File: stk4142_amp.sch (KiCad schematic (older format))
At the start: 6 parts

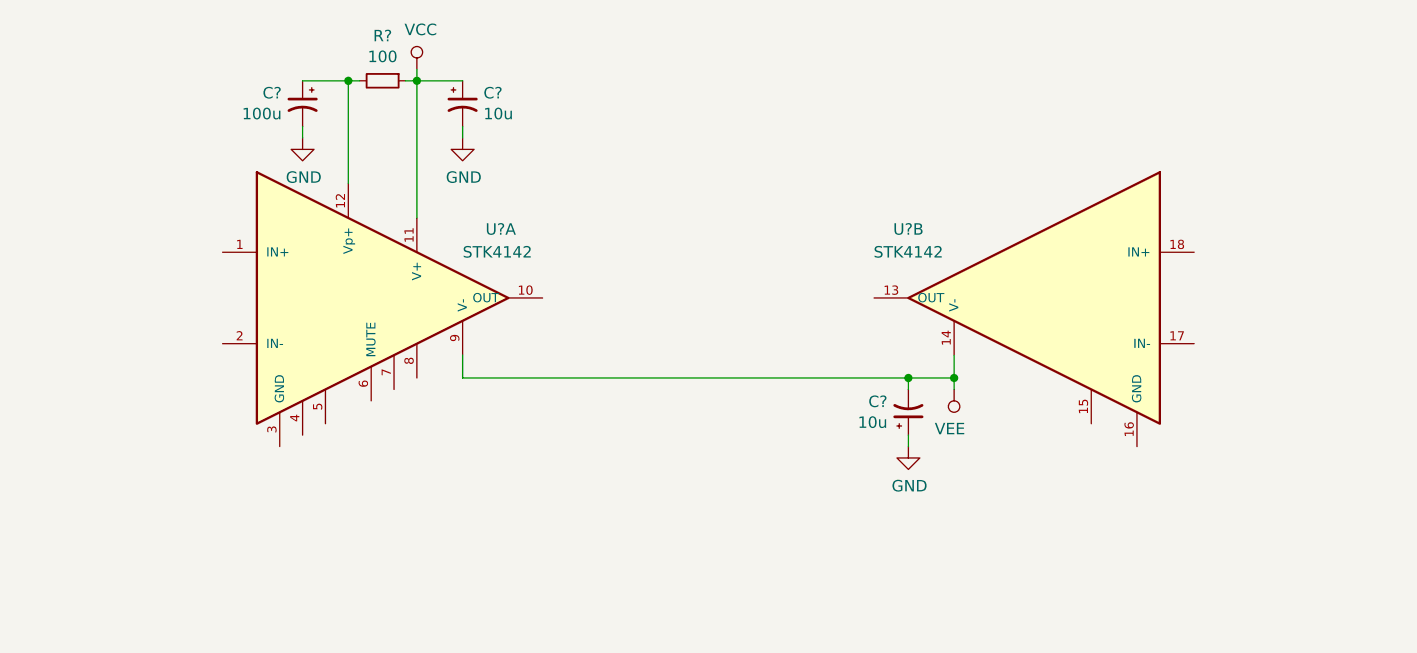
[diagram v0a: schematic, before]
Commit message: main elements of power stage
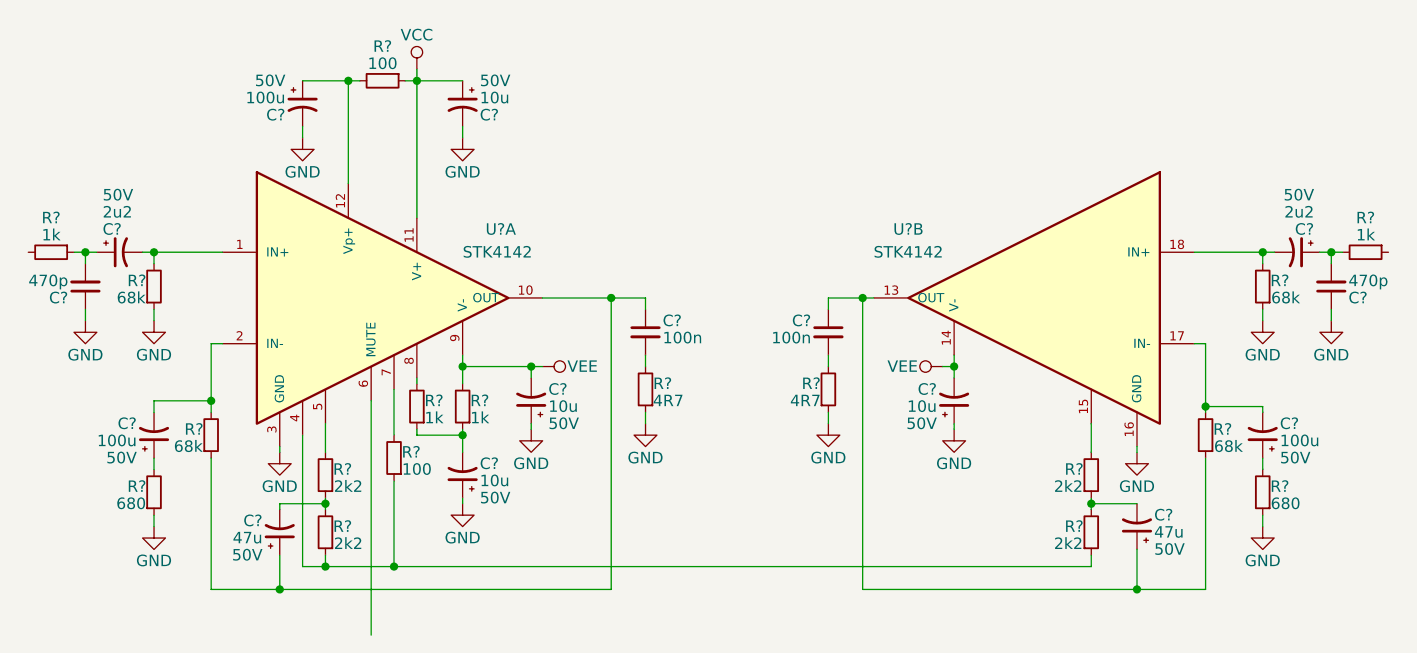
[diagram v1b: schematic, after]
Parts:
- removed C?: 100u, symbol CP1_Small
- removed C? (x2): 10u, symbol CP1_Small
- added C? (x4): 10u, symbol CP1_Small
- added C? (x2): 100n, symbol C_Small
- added C? (x3): 100u, symbol CP1_Small
- added C? (x2): 47u, symbol CP1_Small
- added C? (x2): 470p, symbol C_Small
- added C? (x2): 2u2, symbol CP1_Small
- added R? (x4): 1k, symbol R_Small
- added R?: 100, symbol R_Small
- added R? (x2): 4R7, symbol R_Small
- added R? (x4): 68k, symbol R_Small
- added R? (x4): 2k2, symbol R_Small
- added R? (x2): 680, symbol R_Small
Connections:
- net GND: now also U?.16 (GND), U?.3 (GND), C?.1, C?.1, C?.1, C?.1, C?.1, C?.2, C?.2, R?.1, R?.1, R?.1, R?.1, R?.1, R?.1
- net VCC: now also C?.1
- net VEE: now also C?.2, C?.2, R?.2
- net at U?.1 (IN+): now also C?.2, R?.2
- net at U?.10 (OUT): now also C?.1, C?.1, R?.1
- net at R?.2, U?.12 (Vp+): now also C?.1
- net at U?.2 (IN-): now also C?.2, R?.2
- net at U?.4: now also R?.1, R?.1, R?.1
- net at U?.5: now also R?.2
- net at U?.7: now also R?.2
- net at U?.8: now also R?.2
- net at U?.13 (OUT): now also C?.1, C?.1, R?.1
- net at U?.15: now also R?.2
- net at U?.17 (IN-): now also C?.2, R?.2
- net at U?.18 (IN+): now also C?.2, R?.2
- new net: C?.2, R?.1, R?.1
- new net: C?.2, R?.2 (x2)
- new net: C?.2, R?.1, R?.2 (x2)
- new net: C?.1, R?.2 (x2)
- new net: C?.1, C?.2, R?.1
- new net: C?.1, C?.2, R?.2

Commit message: remap symbols to new KiCad format
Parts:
- C? (x11): symbol CP1_Small -> device:CP1_Small
- C? (x4): symbol C_Small -> device:C_Small
- R? (x18): symbol R_Small -> device:R_Small
- U? (x2): symbol STK4142 -> stk4142_amp-rescue:STK4142-RESCUE-stk4142_amp
